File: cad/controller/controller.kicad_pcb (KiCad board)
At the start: 2 copper layers, 95 x 80 mm, 105 parts, among them J1 RJ45_jack_POE, J2 Barrel_Jack, J3 Conn_02x03_Odd_Even, J4 Conn_01x02, J5 Conn_01x04, J6 Conn_01x05, J7 6P6C, SW1 SW_Push, SW2 SW_Push, U1 NCP1117-5.0_SOT223, U2 NCP1117-3.3_SOT223, U3 CAT811STBI-GT3, U4 W5500, U5 ATmega328-PU, U6 PCA9517A, U7 TXB0104D, Y1 25MHz, Y2 18MHz

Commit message: controller layout
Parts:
- moved R13 166.4 mm to (126.8, 61.9), turned to 270 degrees
- moved R18 162.9 mm to (131.8, 62.2), turned to 90 degrees
- moved R17 162.1 mm to (130.2, 69.0), turned to 270 degrees
- moved C17 161.4 mm to (131.1, 59.5), turned to 180 degrees
- moved R14 160.8 mm to (129.4, 64.9)
- moved R12 159.5 mm to (129.4, 73.0)
- moved J4 159.1 mm to (102.3, 82.2)
- moved R20 159.1 mm to (133.8, 62.2), turned to 90 degrees
- moved R16 157.2 mm to (131.9, 69.0), turned to 270 degrees
- moved R15 155.6 mm to (129.4, 71.4)
- moved R11 154.6 mm to (129.4, 66.5)
- moved C23 152.0 mm to (134.6, 70.0), turned to 180 degrees
- moved R19 151.5 mm to (134.6, 68.3), turned to 180 degrees
- moved C21 151.1 mm to (134.6, 66.5), turned to 180 degrees
- moved C20 148.9 mm to (134.6, 64.8), turned to 180 degrees
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
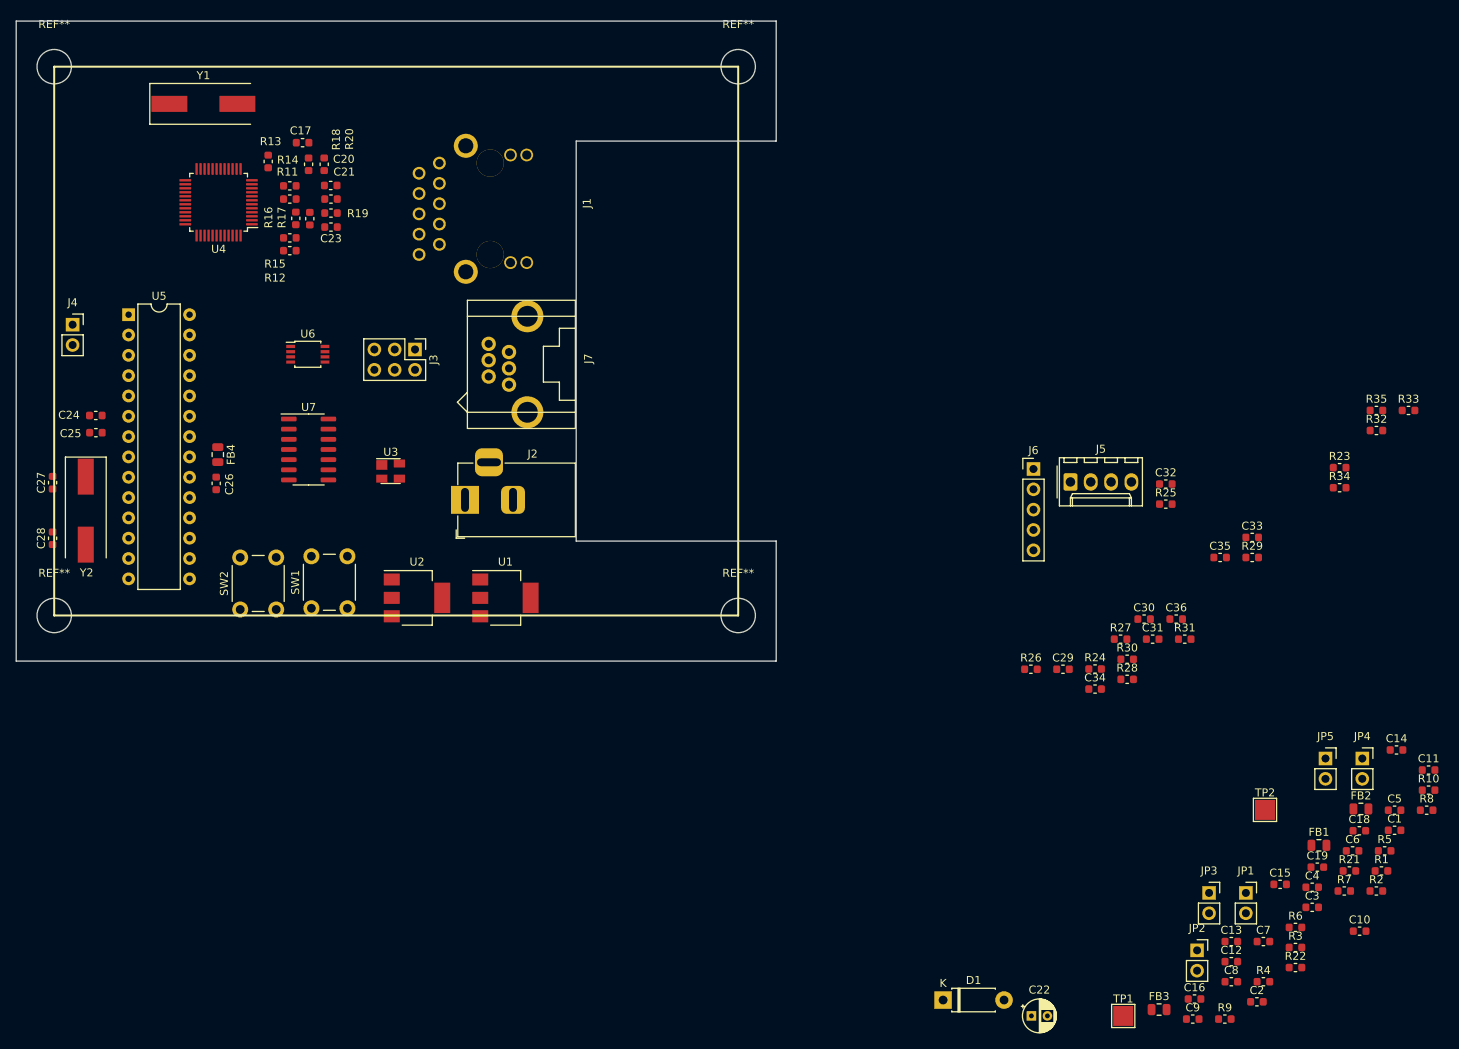
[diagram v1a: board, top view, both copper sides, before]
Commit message: Continued controller board placement
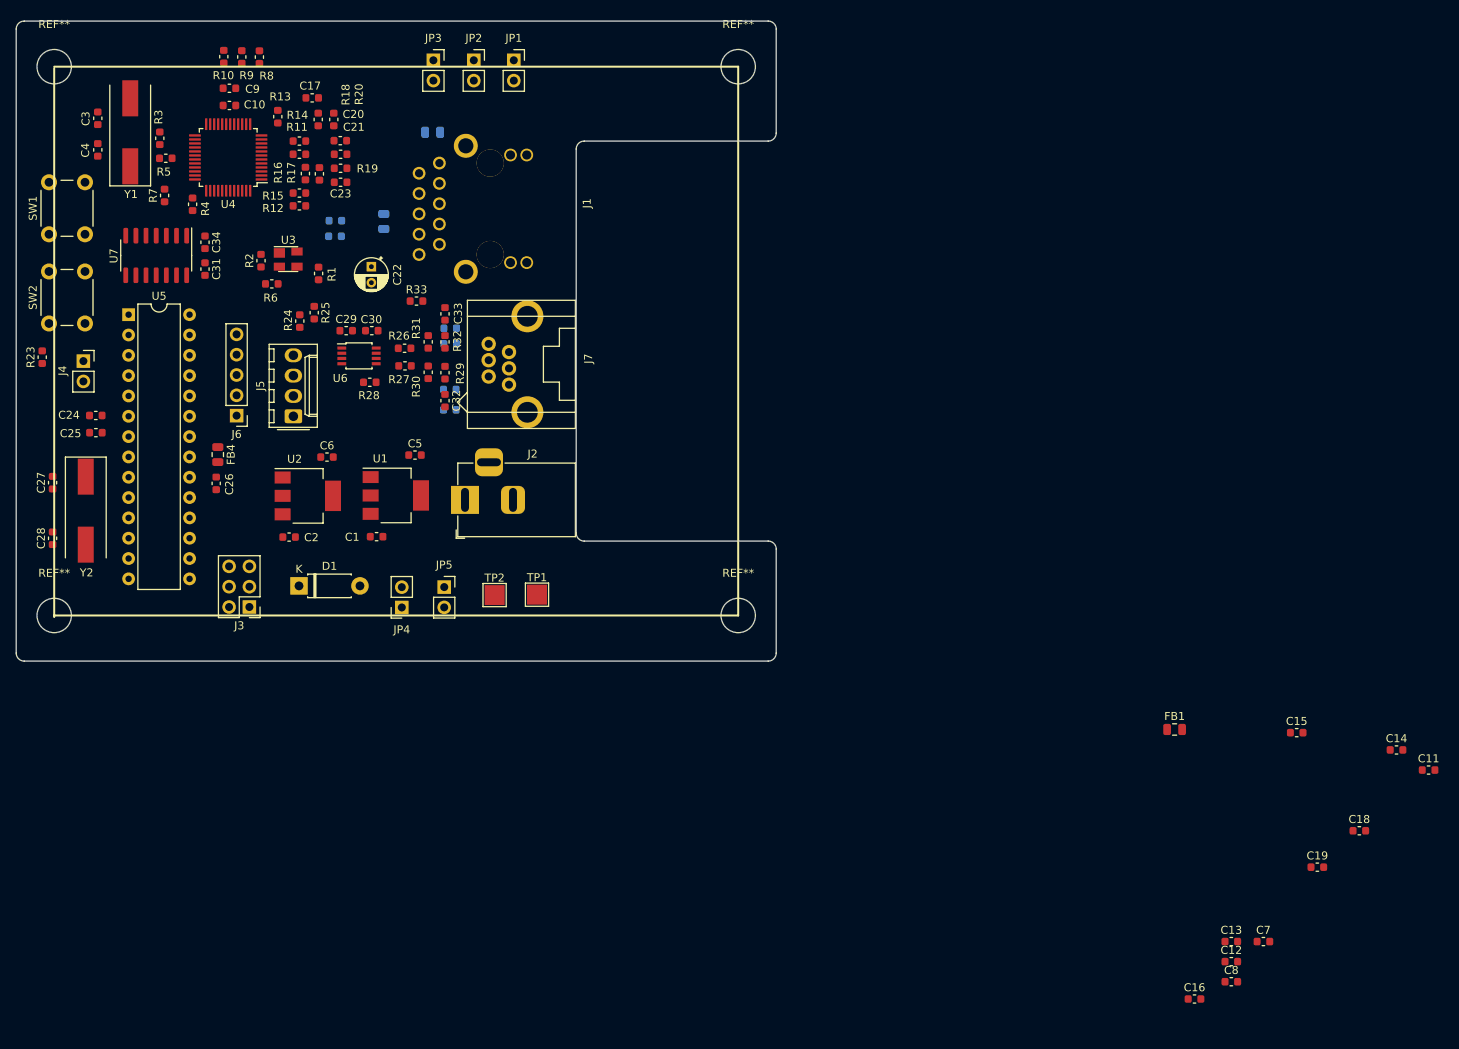
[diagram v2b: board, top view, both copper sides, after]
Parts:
- C35, C36, FB2, FB3, R21, R22, R34, R35: moved to B.Cu
- moved C3 181.0 mm to (105.5, 56.5), turned to 270 degrees
- moved C4 177.6 mm to (105.5, 60.4), turned to 270 degrees
- moved R10 176.3 mm to (121.2, 48.8), turned to 270 degrees
- moved R5 175.2 mm to (114.0, 61.5)
- moved C10 175.0 mm to (121.9, 54.9)
- moved R3 174.3 mm to (113.2, 59.0), turned to 90 degrees
- moved R8 173.6 mm to (125.7, 48.8), turned to 270 degrees
- moved R9 171.9 mm to (123.5, 48.8), turned to 270 degrees
- moved R7 171.2 mm to (113.8, 66.1), turned to 90 degrees
- moved C9 167.4 mm to (121.9, 52.7)
- moved R4 165.4 mm to (117.3, 67.2), turned to 270 degrees
- moved R23 162.8 mm to (98.5, 86.3), turned to 90 degrees
- moved R2 160.1 mm to (125.8, 74.2), turned to 90 degrees
- moved R1 152.4 mm to (133.1, 75.8), turned to 90 degrees
- moved R6 151.1 mm to (127.2, 77.2)
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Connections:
- C24 pad 1: /MCU/5V0 -> 5V0
- C25 pad 1: /MCU/5V0 -> 5V0
- C29 pad 1: /MCU/5V0 -> 5V0
- C30 pad 1: /MCU/3V3 -> 3V3
- C31 pad 2: /MCU/5V0 -> 5V0
- C34 pad 1: /MCU/3V3 -> 3V3
- C35 pad 1: /MCU/3V3 -> 3V3
- C36 pad 1: /MCU/3V3 -> 3V3
- C5 pad 2: /5V0 -> 5V0
- C6 pad 2: /3V3 -> 3V3
- C7 pad 2: /3V3 -> 3V3
- C8 pad 2: /3V3 -> 3V3
- FB1 pad 1: /3V3 -> 3V3
- FB4 pad 1: /MCU/5V0 -> 5V0
- J3 pad 2: /MCU/5V0 -> 5V0
- J5 pad 2: /MCU/3V3 -> 3V3
- J7 pad 5: /MCU/3V3 -> 3V3
- JP2 pad 1: Net-(JP1-Pad1) -> Net-(JP2-Pad1)
- R10 pad 1: Net-(JP1-Pad1) -> Net-(JP2-Pad1)
- R10 pad 2: /3V3 -> 3V3
- R23 pad 1: /MCU/5V0 -> 5V0
- R24 pad 1: /MCU/5V0 -> 5V0
- R25 pad 1: /MCU/5V0 -> 5V0
- R28 pad 1: /MCU/3V3 -> 3V3
- R30 pad 1: /MCU/3V3 -> 3V3
- R31 pad 1: /MCU/3V3 -> 3V3
- R4 pad 2: /3V3 -> 3V3
- R7 pad 1: /CS -> CS
- R8 pad 2: /3V3 -> 3V3
- R9 pad 2: /3V3 -> 3V3
- U1 pad 2: /5V0 -> 5V0
- U2 pad 2: /3V3 -> 3V3
- U3 pad 4: /3V3 -> 3V3
- U4 pad 28: /3V3 -> 3V3
- U4 pad 33: /SCLK -> SCLK
- U4 pad 34: /MISO -> MISO
- U4 pad 35: /MOSI -> MOSI
- U4 pad 43: Net-(JP1-Pad1) -> Net-(JP2-Pad1)
- U5 pad 7: /MCU/5V0 -> 5V0
- U6 pad 1: /MCU/5V0 -> 5V0
- U6 pad 8: /MCU/3V3 -> 3V3
- U7 pad 1: /MCU/3V3 -> 3V3
- U7 pad 14: /MCU/5V0 -> 5V0
- U7 pad 2: /MCU/SCLK -> SCLK
- U7 pad 3: /MCU/MISO -> MISO
- U7 pad 4: /MCU/MOSI -> MOSI
- U7 pad 5: /MCU/CS -> CS
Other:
- outline, holes or cut-outs redrawn

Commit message: Finished placement of controller
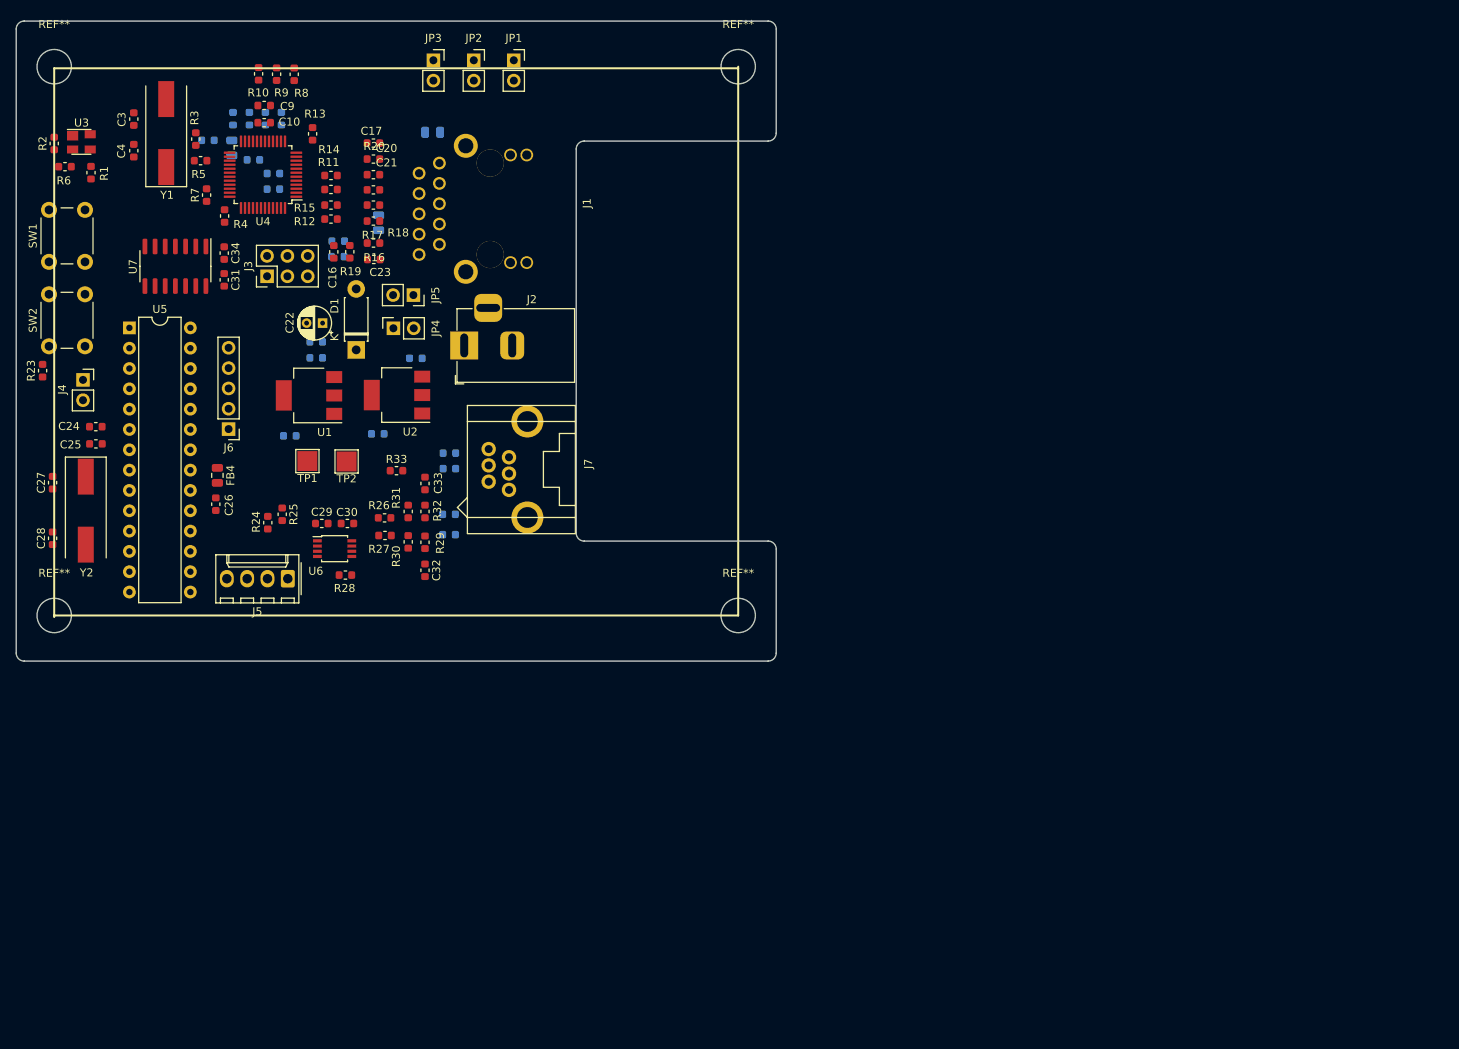
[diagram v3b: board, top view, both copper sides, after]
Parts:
- C1, C11, C12, C13, C14, C15, C18, C19, C2, C5, C6, C7, C8, FB1: moved to B.Cu
- moved C11 168.4 mm to (124.4, 56.5), turned to 270 degrees
- moved C18 167.8 mm to (119.2, 59.2)
- moved C7 164.8 mm to (122.3, 56.5), turned to 270 degrees
- moved C12 160.3 mm to (126.4, 56.5), turned to 270 degrees
- moved C8 159.7 mm to (124.9, 61.6), turned to 180 degrees
- moved C14 157.8 mm to (127.4, 63.4)
- moved C13 157.1 mm to (128.4, 56.5), turned to 270 degrees
- moved C15 144.8 mm to (127.4, 65.3)
- moved C16 142.5 mm to (134.9, 73.2), turned to 90 degrees
- moved C19 141.3 mm to (132.8, 84.4), turned to 180 degrees
- moved FB1 138.5 mm to (122.2, 60.1), turned to 90 degrees
- moved J3 41.4 mm to (126.6, 76.2), turned to 90 degrees
- moved JP5 36.7 mm to (144.9, 78.5), turned to 270 degrees
- moved JP4 34.9 mm to (142.4, 82.7), turned to 90 degrees
- moved TP1 33.2 mm to (131.7, 99.3), turned to 180 degrees
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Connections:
- C12 pad 1: Net-(C12-Pad1) -> GND
- C13 pad 1: Net-(C13-Pad1) -> GND
- C14 pad 1: Net-(C14-Pad1) -> GND
- C15 pad 1: Net-(C15-Pad1) -> GND
- C19 pad 1: /PIN_12V_POE -> /PIN_12V
- C22 pad 1: /PIN_12V_POE -> /PIN_12V
- FB2 pad 1: /PIN_12V_POE -> Net-(FB2-Pad1)
- JP5 pad 1: /PIN_12V_POE -> Net-(FB2-Pad1)
- TP2 pad 1: /PIN_12V_POE -> /PIN_12V
- U7 pad 7: Net-(U7-Pad7) -> GND
- U7 pad 8: Net-(U7-Pad8) -> GND

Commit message: Began routing controller
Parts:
- moved FB2 11.9 mm to (148.4, 78.4)
- moved R23 10.6 mm to (107.1, 81.8), turned to 270 degrees
- moved J4 4.60 mm to (108.2, 89.8)
- moved C27 3.75 mm to (103.5, 102.0)
- moved C28 3.75 mm to (103.5, 109.0)
- moved J5 3.27 mm to (132.4, 113.6)
- moved C24 3.23 mm to (108.4, 95.5)
- moved C25 3.19 mm to (108.4, 97.2)
- moved SW1 3.15 mm to (99.3, 71.2)
- moved SW2 3.15 mm to (99.3, 81.8)
- moved Y2 3.15 mm to (107.1, 105.5)
- moved C5 3.13 mm to (130.8, 93.3), turned to 90 degrees
- moved C6 2.98 mm to (141.9, 93.3), turned to 90 degrees
- moved U6 2.67 mm to (135.4, 107.6)
- moved C29 2.67 mm to (133.8, 104.5)
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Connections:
- J1 pad 2: Net-(J1-Pad2) -> Net-(FB3-Pad2)
- J1 pad 7: Net-(J1-Pad7) -> Net-(FB2-Pad2)
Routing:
- net /MCU/CS_5V: track 0.00 -> 38.0 mm
- net /MCU/MOSI_5V: track 0.00 -> 34.9 mm
- net /MCU/MISO_5V: track 0.00 -> 31.9 mm
- net /MCU/SCLK_5V: track 0.00 -> 28.7 mm
- net 5V0: track 0.00 -> 24.5 mm, vias 0 -> 25
- net Net-(J1-Pad10): track 0.00 -> 17.3 mm
- net /MCU/RST: track 0.00 -> 14.8 mm
- net Net-(FB2-Pad2): track 0.00 -> 13.5 mm
- net Net-(C23-Pad1): track 0.00 -> 13.4 mm
- net Net-(C20-Pad1): track 0.00 -> 13.2 mm
- net Net-(C17-Pad1): track 0.00 -> 12.9 mm, vias 0 -> 2
- net Net-(J1-Pad8): track 0.00 -> 11.7 mm
- net Net-(C21-Pad1): track 0.00 -> 11.0 mm
- net /PIN_12V_JACK: track 0.00 -> 9.59 mm
- net Net-(FB3-Pad2): track 0.00 -> 7.33 mm
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- added copper zone on B.Cu, net /PIN_12V
- added copper zone on F.Cu, net /PIN_12V
- added copper zone on B.Cu, net 5V0
- added copper zone on F.Cu, net 5V0
- added copper zone on B.Cu, net Net-(D1-Pad2)
- added copper zone on F.Cu, net Net-(J1-Pad10)
- added copper zone on F.Cu, net Net-(J1-Pad8)

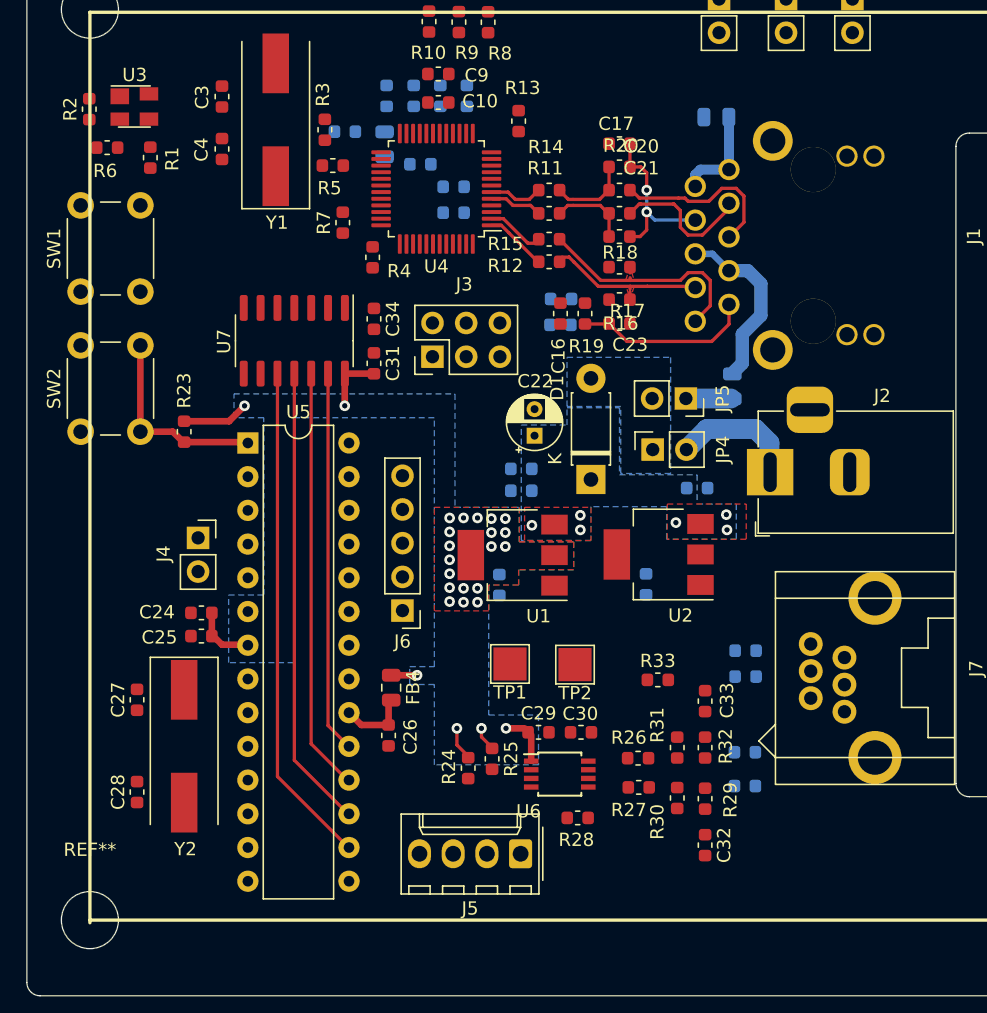
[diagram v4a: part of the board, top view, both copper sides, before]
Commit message: Continued controller routing
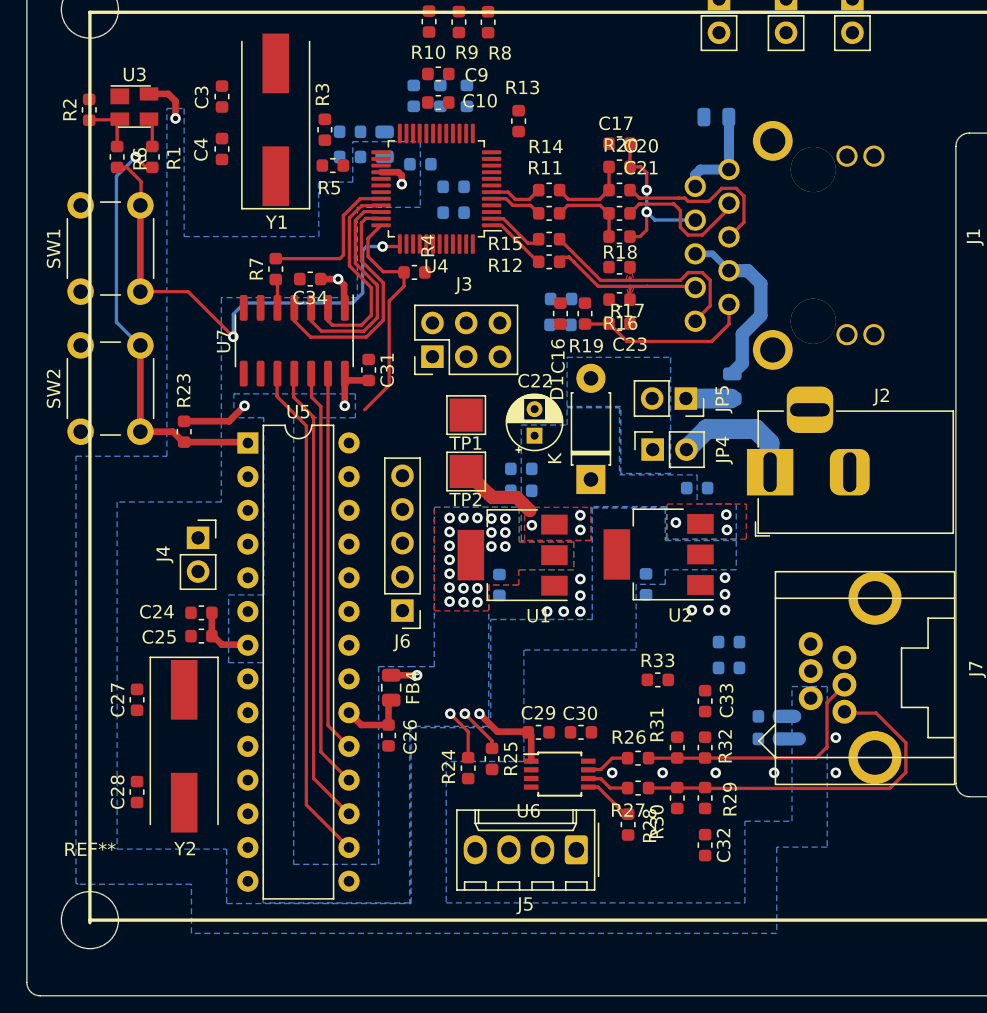
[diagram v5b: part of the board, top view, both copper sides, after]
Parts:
- moved TP1 19.0 mm to (128.3, 80.5)
- moved TP2 16.7 mm to (128.3, 84.8)
- moved R7 6.14 mm to (114.0, 69.5)
- moved C34 5.66 mm to (116.6, 70.3), turned to 180 degrees
- moved C7 5.36 mm to (119.6, 61.1), turned to 0 degrees
- moved J5 4.21 mm to (136.7, 113.3)
- moved C36 3.98 mm to (151.2, 105.0)
- moved R28 3.83 mm to (140.6, 111.4), turned to 90 degrees
- moved R4 3.35 mm to (124.5, 69.8), turned to 0 degrees
- moved C35 3.24 mm to (151.2, 103.2)
- moved R34 1.41 mm to (148.2, 99.6)
- moved R35 1.41 mm to (148.2, 97.7)
- moved R6 1.03 mm to (102.0, 61.1), turned to 90 degrees
- moved C31 0.64 mm to (121.0, 77.2)
- moved C18 0.39 mm to (119.6, 59.2)
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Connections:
- J3 pad 5: /MCU/RST -> RST
- R1 pad 1: /RST -> RST
- R23 pad 2: /MCU/RST -> RST
- SW2 pad 2: /MCU/RST -> RST
- U5 pad 1: /MCU/RST -> RST
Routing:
- net /RST_W5500: track 0.00 -> 37.1 mm, vias 0 -> 2
- net RST: track 0.00 -> 31.9 mm, vias 0 -> 1
- net /MCU/SDA_RJ11: track 0.00 -> 27.6 mm
- net /MCU/SCL_RJ11: track 0.00 -> 19.0 mm
- net MOSI: track 0.00 -> 18.1 mm
- net /INT_W5500: track 0.00 -> 17.5 mm
- net MISO: track 0.00 -> 16.8 mm
- net SCLK: track 0.00 -> 15.2 mm
- net /MCU/RST: track 14.8 -> 0.00 mm
- net 3V3: track 0.00 -> 11.8 mm, vias 0 -> 3
- net Net-(R7-Pad2): track 0.00 -> 11.2 mm
- net /PIN_12V: track 0.00 -> 6.02 mm
- net 5V0: track 24.5 -> 29.8 mm
- net Net-(R2-Pad1): track 0.00 -> 4.08 mm
- net Net-(R28-Pad2): track 0.00 -> 3.81 mm
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- added copper zone on B.Cu, net 3V3
